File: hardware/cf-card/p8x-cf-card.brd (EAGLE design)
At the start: 160 x 100 mm, 27 parts, among them J1 FABC96R, J2 CF/IDE 40P, U1 DATA BUF, U2 IO PAGE, U3 DOE DEC, U4 DLD DEC, U5 74HCT14, U6 74HCT10, U7 74HCT10, U8 74HCT08, U9 CF HI-BYTE DNP

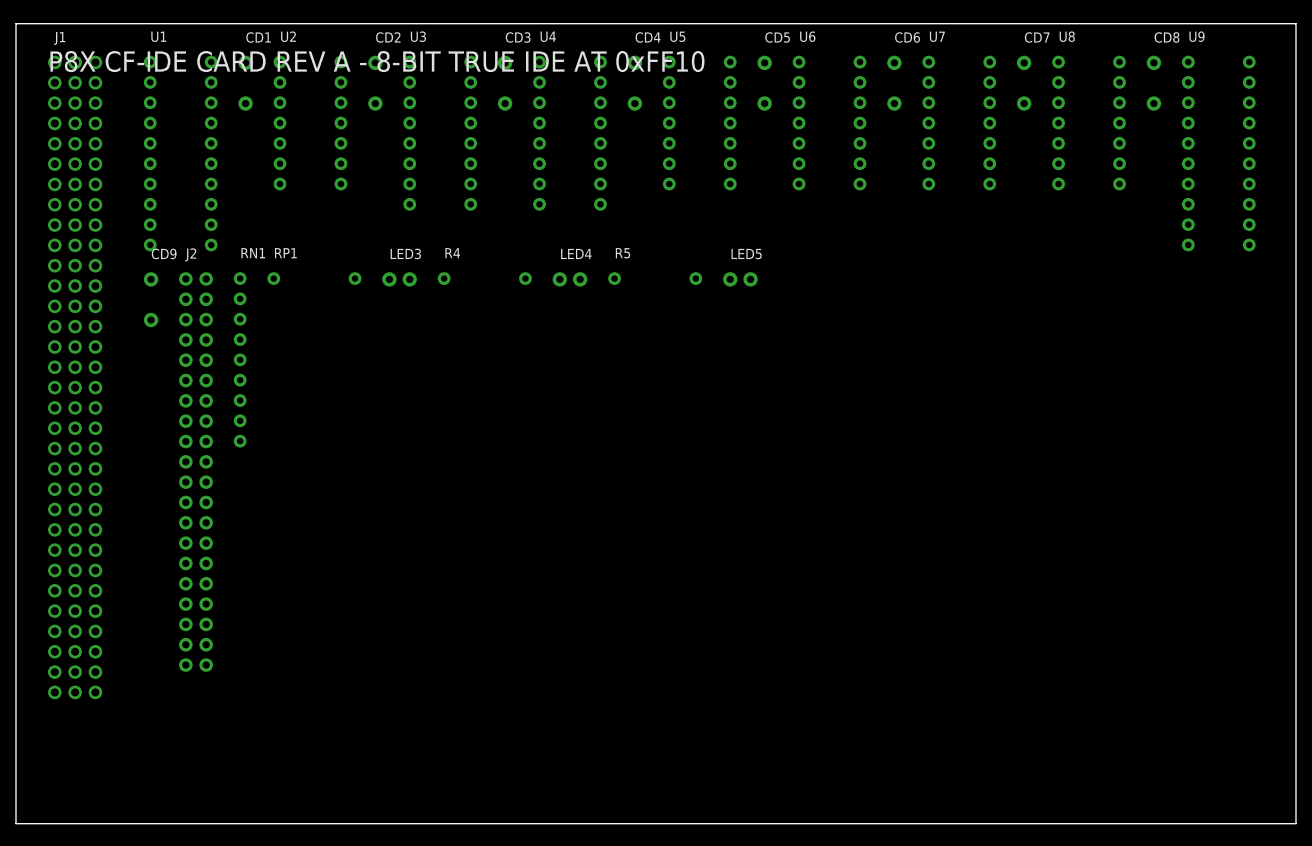
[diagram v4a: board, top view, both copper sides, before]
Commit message: feat(hw): card DIN connector mounting holes (DIN96C, standard DIN 41612)
The card edge connector (FABC96R) needs board mounting holes; the footprint had
only the 96 signal pins. Split the connector into two packages so cards and the
backplane don't share holes:
- DIN96C (card): 96 pins + 2 mounting holes on the centreline (x=2.54), 94.0mm
  apart, drill 2.8mm for M2.5. Emitted as non-plated <hole> elements (new
  lib_xml branch for MH* entries). DEV["DIN96C"] = DIN96 pins, pkg DIN96C.
- DIN96 (backplane receptacle): pins only, unchanged.
Card J1 (all 6: 5 plug-in via card() + memory) now uses DIN96C; backplane slots
keep DIN96. Fixed card() to honor the J1 package on the board side and in CARDS
(was hardcoding "DIN96", which both dropped the holes and mislabeled the BOM).

Verified: each card .brd has 2 holes, backplane 0; overlap guard clean (the
shared-package version collided with backplane terminators); BOM shows 6 card
(DIN96C) + 10 backplane. All boards 0 errors, all 6 suites pass.

VERIFY the 94mm spacing / 2.8mm dia against the FABC96R datasheet.

Co-Authored-By: Claude Opus 4.8 <noreply@anthropic.com>
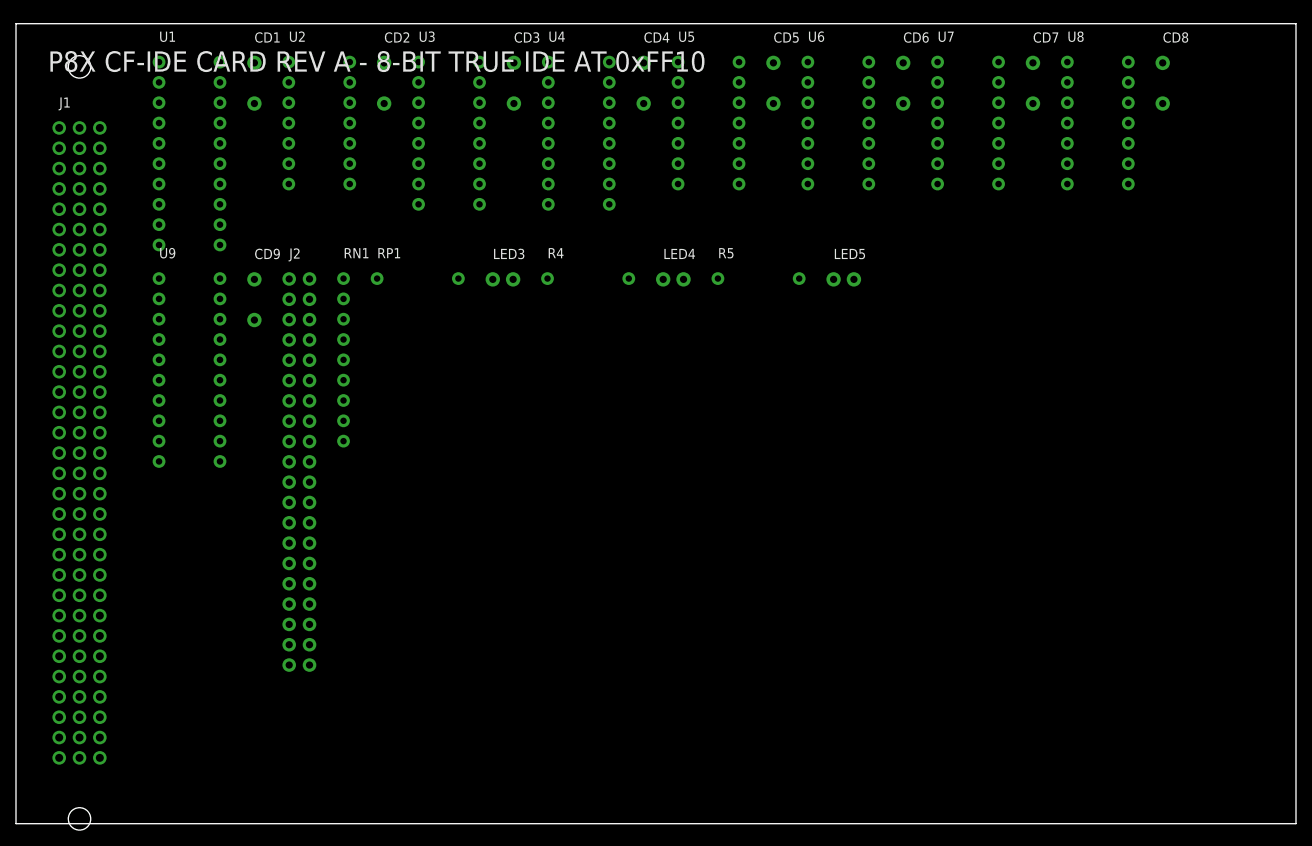
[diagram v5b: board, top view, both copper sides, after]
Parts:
- J1: device p8x:DIN96 -> p8x:DIN96C
- moved U9 131.5 mm to (17.9, 68.1)
- moved CD9 12.9 mm to (29.8, 68.0)
- moved LED3 12.9 mm to (59.6, 68.0)
- moved LED4 12.9 mm to (80.9, 68.0)
- moved LED5 12.9 mm to (102.2, 68.0)
- moved R5 12.9 mm to (87.7, 68.1)
- moved RP1 12.9 mm to (45.1, 68.1)
- moved J2 12.9 mm to (34.1, 68.1)
- moved RN1 12.9 mm to (40.9, 68.1)
- moved R4 12.9 mm to (66.4, 68.1)
- moved J1 8.20 mm to (5.40, 87.0)
- moved CD5 1.10 mm to (94.7, 95.1)
- moved CD6 1.10 mm to (110.9, 95.1)
- moved CD7 1.10 mm to (127.1, 95.1)
- moved U4 1.10 mm to (66.5, 95.2)
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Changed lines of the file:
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@@
 <designrules name="default"><param name="layerSetup" value="(1*2*15*16)"/></designrules>
 <elements>
-<element name="J1" library="p8x" package="DIN96" value="FABC96R" x="4.85" y="95.15"/>
-<element name="U1" library="p8x" package="DIP20" value="DATA BUF" x="16.78" y="95.20"/>
-<element name="CD1" library="p8x" package="C_DISC" value="100N" x="28.70" y="95.10"/>
-<element name="U2" library="p8x" package="DIP14" value="IO PAGE" x="33.00" y="95.20"/>
-<element name="CD2" library="p8x" package="C_DISC" value="100N" x="44.92" y="95.10"/>
-<element name="U3" library="p8x" package="DIP16" value="DOE DEC" x="49.22" y="95.20"/>
-<element name="CD3" library="p8x" package="C_DISC" value="100N" x="61.14" y="95.10"/>
-<element name="U4" library="p8x" package="DIP16" value="DLD DEC" x="65.44" y="95.20"/>
-<element name="CD4" library="p8x" package="C_DISC" value="100N" x="77.36" y="95.10"/>
-<element name="U5" library="p8x" package="DIP14" value="74HCT14" x="81.66" y="95.20"/>
-<element name="CD5" library="p8x" package="C_DISC" value="100N" x="93.58" y="95.10"/>
-<element name="U6" library="p8x" package="DIP14" value="74HCT10" x="97.88" y="95.20"/>
-<element name="CD6" library="p8x" package="C_DISC" value="100N" x="109.80" y="95.10"/>
-<element name="U7" library="p8x" package="DIP14" value="74HCT10" x="114.10" y="95.20"/>
-<element name="CD7" library="p8x" package="C_DISC" value="100N" x="126.02" y="95.10"/>
-<element name="U8" library="p8x" package="DIP14" value="74HCT08" x="130.32" y="95.20"/>
-<element name="CD8" library="p8x" package="C_DISC" value="100N" x="142.24" y="95.10"/>
-<element name="U9" library="p8x" package="DIP20" value="CF HI-BYTE DNP" x="146.54" y="95.20"/>
-<element name="CD9" library="p8x" package="C_DISC" value="100N" x="16.88" y="68.04"/>
-<element name="J2" library="p8x" package="HDR40" value="CF/IDE 40P" x="21.23" y="68.09"/>
-<element name="RN1" library="p8x" package="SIP9" value="8X10K" x="28.02" y="68.14"/>
-<element name="RP1" library="p8x" package="R_AXIAL" value="1K" x="32.22" y="68.14"/>
-<element name="LED3" library="p8x" package="LED5" value="PWR-GRN" x="46.68" y="68.04"/>
-<element name="R4" library="p8x" package="R_AXIAL" value="1K" x="53.52" y="68.14"/>
-<element name="LED4" library="p8x" package="LED5" value="ACT-YEL" x="67.98" y="68.04"/>
-<element name="R5" library="p8x" package="R_AXIAL" value="330R" x="74.82" y="68.14"/>
-<element name="LED5" library="p8x" package="LED5" value="DASP-GRN" x="89.28" y="68.04"/>
+<element name="J1" library="p8x" package="DIN96C" value="FABC96R" x="5.40" y="86.97"/>
+<element name="U1" library="p8x" package="DIP20" value="DATA BUF" x="17.88" y="95.20"/>
+<element name="CD1" library="p8x" package="C_DISC" value="100N" x="29.80" y="95.10"/>
+<element name="U2" library="p8x" package="DIP14" value="IO PAGE" x="34.10" y="95.20"/>
+<element name="CD2" library="p8x" package="C_DISC" value="100N" x="46.02" y="95.10"/>
+<element name="U3" library="p8x" package="DIP16" value="DOE DEC" x="50.32" y="95.20"/>
+<element name="CD3" library="p8x" package="C_DISC" value="100N" x="62.24" y="95.10"/>
+<element name="U4" library="p8x" package="DIP16" value="DLD DEC" x="66.54" y="95.20"/>
+<element name="CD4" library="p8x" package="C_DISC" value="100N" x="78.46" y="95.10"/>
+<element name="U5" library="p8x" package="DIP14" value="74HCT14" x="82.76" y="95.20"/>
+<element name="CD5" library="p8x" package="C_DISC" value="100N" x="94.68" y="95.10"/>
+<element name="U6" library="p8x" package="DIP14" value="74HCT10" x="98.98" y="95.20"/>
+<element name="CD6" library="p8x" package="C_DISC" value="100N" x="110.90" y="95.10"/>
+<element name="U7" library="p8x" package="DIP14" value="74HCT10" x="115.20" y="95.20"/>
+<element name="CD7" library="p8x" package="C_DISC" value="100N" x="127.12" y="95.10"/>
+<element name="U8" library="p8x" package="DIP14" value="74HCT08" x="131.42" y="95.20"/>
+<element name="CD8" library="p8x" package="C_DISC" value="100N" x="143.34" y="95.10"/>
+<element name="U9" library="p8x" package="DIP20" value="CF HI-BYTE DNP" x="17.88" y="68.14"/>
+<element name="CD9" library="p8x" package="C_DISC" value="100N" x="29.80" y="68.04"/>
+<element name="J2" library="p8x" package="HDR40" value="CF/IDE 40P" x="34.15" y="68.09"/>
+<element name="RN1" library="p8x" package="SIP9" value="8X10K" x="40.94" y="68.14"/>
+<element name="RP1" library="p8x" package="R_AXIAL" value="1K" x="45.14" y="68.14"/>
+<element name="LED3" library="p8x" package="LED5" value="PWR-GRN" x="59.60" y="68.04"/>
+<element name="R4" library="p8x" package="R_AXIAL" value="1K" x="66.44" y="68.14"/>
+<element name="LED4" library="p8x" package="LED5" value="ACT-YEL" x="80.90" y="68.04"/>
+<element name="R5" library="p8x" package="R_AXIAL" value="330R" x="87.74" y="68.14"/>
+<element name="LED5" library="p8x" package="LED5" value="DASP-GRN" x="102.20" y="68.04"/>
 </elements><signals>
 <signal name="-CFOE">

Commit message: fix(hardware): connect IC power pins on the card()-built boards
Schematic-review fix. card() wired the edge-connector and decoupling-cap pins to
VCC/GND but never added each IC's own VCC/GND supply pin, so on control, regbank,
ALU, I/O, and CF the chips' power pads were not members of the power pours and
would not have been powered. (The hand-built memory card already did this; the
backplane has no ICs. validate() couldn't catch it — it checks pin-name legality,
not connectivity.)

- card(): append (ref,"VCC")/(ref,"GND") for every IC, skipping any pin already
  wired by hand (idempotent — avoids duplicate pinrefs, e.g. ALU U16 GND)
- regenerated all 7 boards (.sch/.brd), 0 validation errors
- board-level audit: every IC on every card now has both VCC and GND on the
  power signals
- BACKLOG: moved the critical item to DONE; theory docs' power-pin callouts
  updated to "fixed"

Co-Authored-By: Claude Opus 4.8 <noreply@anthropic.com>
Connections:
- net GND: now also U1.10, U2.7, U3.8, U4.8, U5.7, U6.7, U7.7, U8.7, U9.10
- net VCC: now also U1.20, U2.14, U3.16, U4.16, U5.14, U6.14, U7.14, U8.14, U9.20
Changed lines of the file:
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@@
 <contactref element="CD8" pad="2"/>
 <contactref element="CD9" pad="2"/>
+<contactref element="U1" pad="10"/>
+<contactref element="U2" pad="7"/>
+<contactref element="U3" pad="8"/>
+<contactref element="U4" pad="8"/>
+<contactref element="U5" pad="7"/>
+<contactref element="U6" pad="7"/>
+<contactref element="U7" pad="7"/>
+<contactref element="U8" pad="7"/>
+<contactref element="U9" pad="10"/>
 <polygon width="0.254" layer="2" isolate="0.3" rank="1">
 <vertex x="0" y="0"/>
@@
 <contactref element="CD8" pad="1"/>
 <contactref element="CD9" pad="1"/>
+<contactref element="U1" pad="20"/>
+<contactref element="U2" pad="14"/>
+<contactref element="U3" pad="16"/>
+<contactref element="U4" pad="16"/>
+<contactref element="U5" pad="14"/>
+<contactref element="U6" pad="14"/>
+<contactref element="U7" pad="14"/>
+<contactref element="U8" pad="14"/>
+<contactref element="U9" pad="20"/>
 <polygon width="0.254" layer="15" isolate="0.3" rank="1">
 <vertex x="0" y="0"/>

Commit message: feat(backplane): row-B even pins become spare bus lines (SPARE12-23)
Row B was a solid ground guard (B3-26 all GND). Per request, B3-26 now ALTERNATE:
odd pins stay GND (still a guard between most signal pairs), and the 12 even pins
(B4,B6,..,B26) become spare bus lines SPARE12-SPARE23, routed slot-to-slot — so
new signals can be added later without re-spinning the backplane. B27-30
(CLRC/BSEL/IRQ/SPARE11) unchanged.

- busnet() updated in all three copies (gen_eagle, gen_bus_pdf, gen_bus_card)
- backplane .brd routes the 12 new spares (mirrors the B27-30 routing); odd-pin
  grounds remain on the GND pour
- every card regenerated: their connectors no longer tie the even B pins to GND
  (those are spare lines now) — they simply don't connect the spares
- all 8 boards validate (0 errors); schematic + bus PDFs regenerated
- docs updated: bus-definition (pin map + notes), backplane theory + design notes
- net signal-integrity trade noted: a solid guard shields slightly better; the
  alternation was chosen deliberately for expansion room

Co-Authored-By: Claude Opus 4.8 <noreply@anthropic.com>
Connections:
- net GND: no longer J1.B10, J1.B12, J1.B14, J1.B16, J1.B18, J1.B20, J1.B22, J1.B24, J1.B26, J1.B4, J1.B6, J1.B8
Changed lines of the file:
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@@
 <contactref element="J1" pad="A32"/>
 <contactref element="J1" pad="B3"/>
-<contactref element="J1" pad="B4"/>
 <contactref element="J1" pad="B5"/>
-<contactref element="J1" pad="B6"/>
 <contactref element="J1" pad="B7"/>
-<contactref element="J1" pad="B8"/>
 <contactref element="J1" pad="B9"/>
-<contactref element="J1" pad="B10"/>
 <contactref element="J1" pad="B11"/>
-<contactref element="J1" pad="B12"/>
 <contactref element="J1" pad="B13"/>
-<contactref element="J1" pad="B14"/>
 <contactref element="J1" pad="B15"/>
-<contactref element="J1" pad="B16"/>
 <contactref element="J1" pad="B17"/>
-<contactref element="J1" pad="B18"/>
 <contactref element="J1" pad="B19"/>
-<contactref element="J1" pad="B20"/>
 <contactref element="J1" pad="B21"/>
-<contactref element="J1" pad="B22"/>
 <contactref element="J1" pad="B23"/>
-<contactref element="J1" pad="B24"/>
 <contactref element="J1" pad="B25"/>
-<contactref element="J1" pad="B26"/>
 <contactref element="J1" pad="B31"/>
 <contactref element="J1" pad="B32"/>

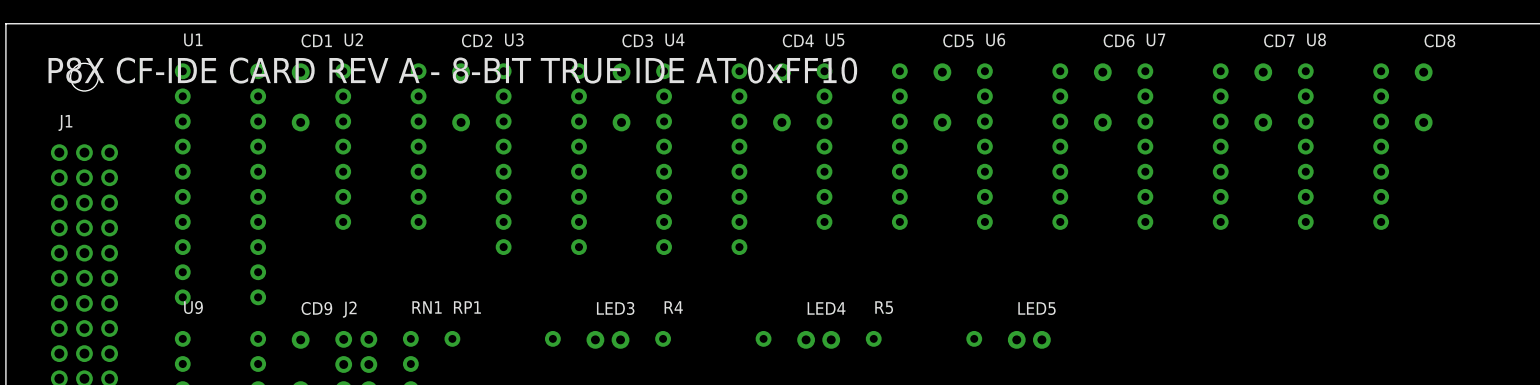
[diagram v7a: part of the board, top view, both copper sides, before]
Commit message: feat(generators): faithful Eagle/Fusion output (values, layers, smashed parts)
Make the generated .sch/.brd match how Eagle itself writes files, so Fusion
displays everything correctly (was mis-mapping names/values to scratch layers):

- devicesets get uservalue="yes" so the `value` field is honored at all (it was
  silently ignored before — no card's value ever displayed)
- emit the COMPLETE standard Eagle layer table (62 layers) in every drawing, so
  Fusion has nothing to remap on import
- board elements are now smashed="yes" with explicit NAME (tNames/25) and VALUE
  (tValues/27) attributes — refdes + part number show reliably
- add std <attributes>/<variantdefs> board sections + board-package >VALUE silk
- schematic: `value` holds the orderable part number (>VALUE + BOM); the logical
  function is placed as text near each chip via a new card() `labels` arg
- write_brd gains outline_only and unplaced modes (parts off-board + ratsnest);
  card() exposes brd_outline_only / brd_unplaced

Proven on the LED card (part numbers + function labels + an unplaced 4-layer
board). The other cards get the structural fixes now; rolling the part-number/
labels convention across them is the next step. All 8 boards validate (0 errors).

Co-Authored-By: Claude Opus 4.8 <noreply@anthropic.com>
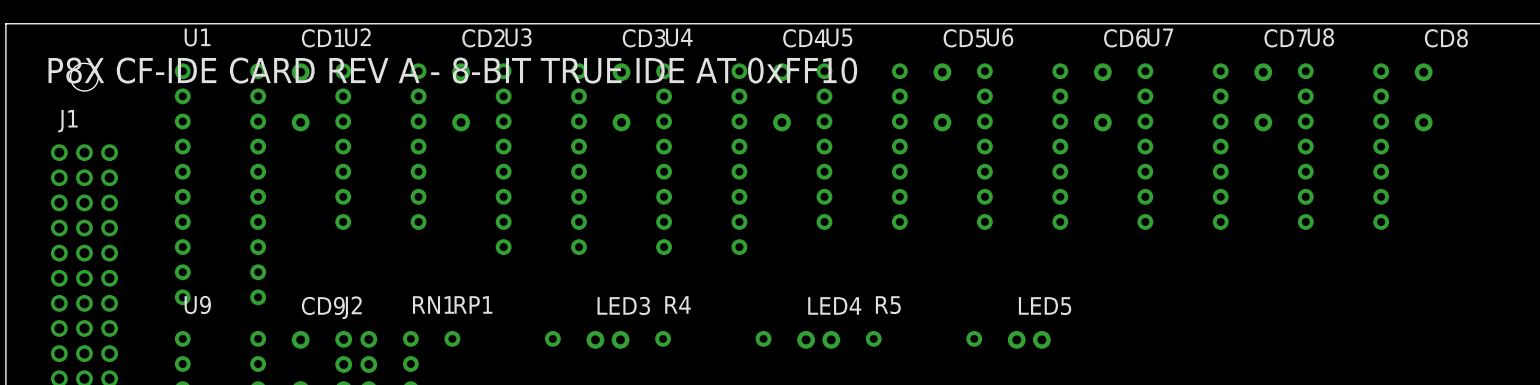
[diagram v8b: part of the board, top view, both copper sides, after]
